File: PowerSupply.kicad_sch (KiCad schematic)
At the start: 18 parts, among them Q2 AO3401A, U4 RT7272BGSP

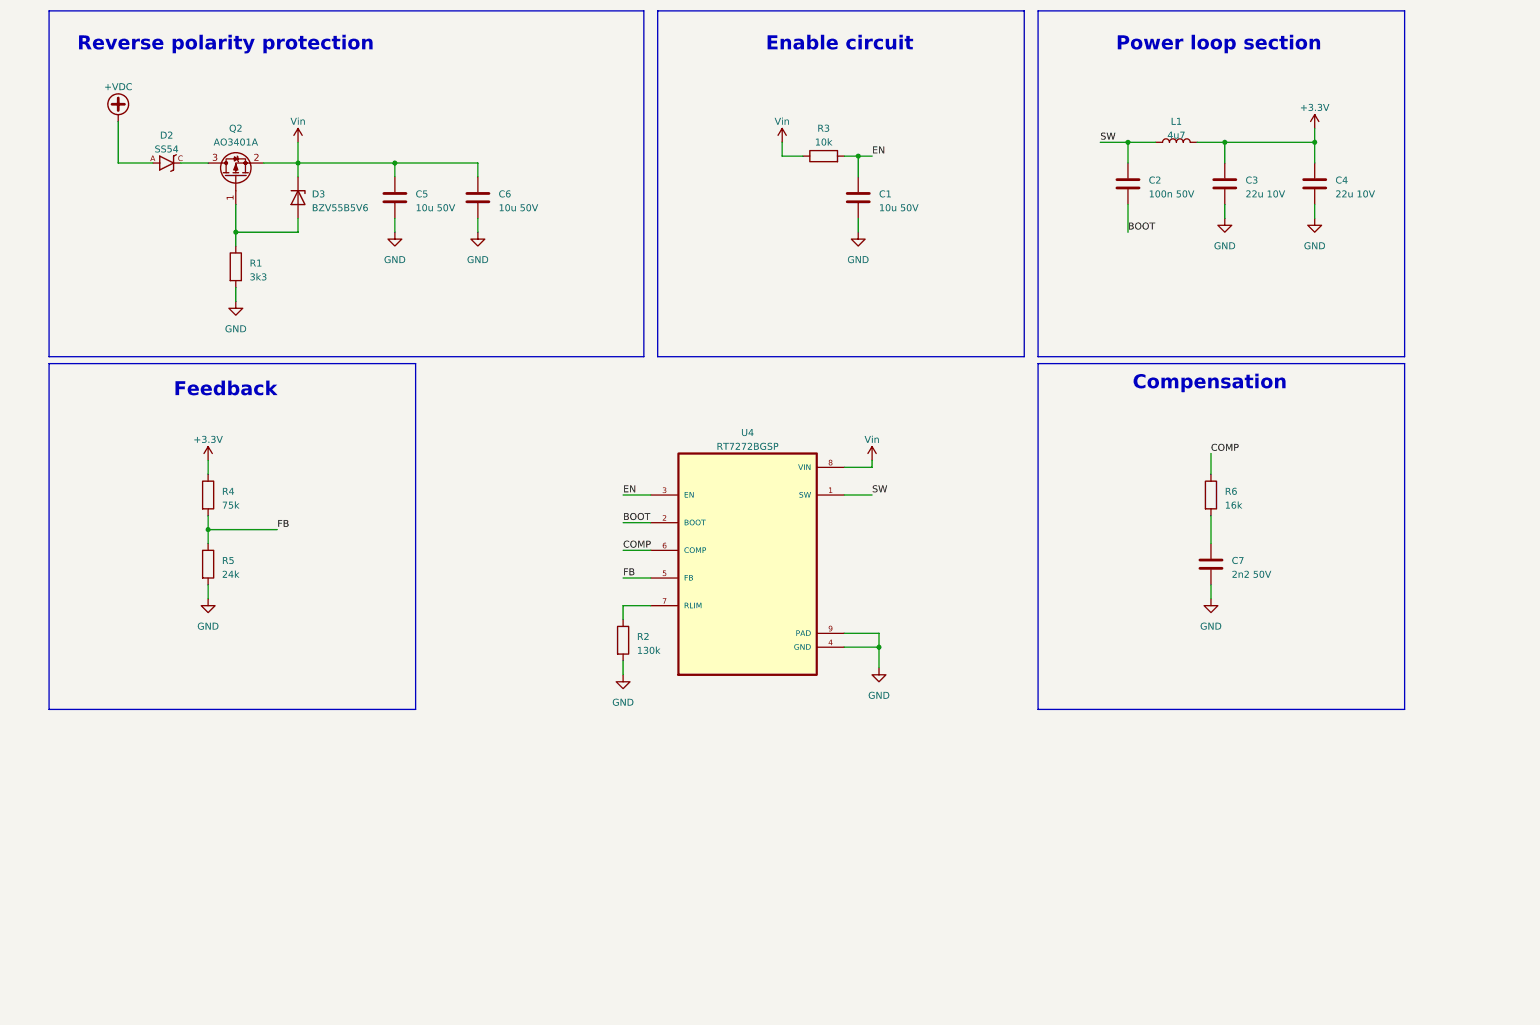
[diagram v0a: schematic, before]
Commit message: All components have been added
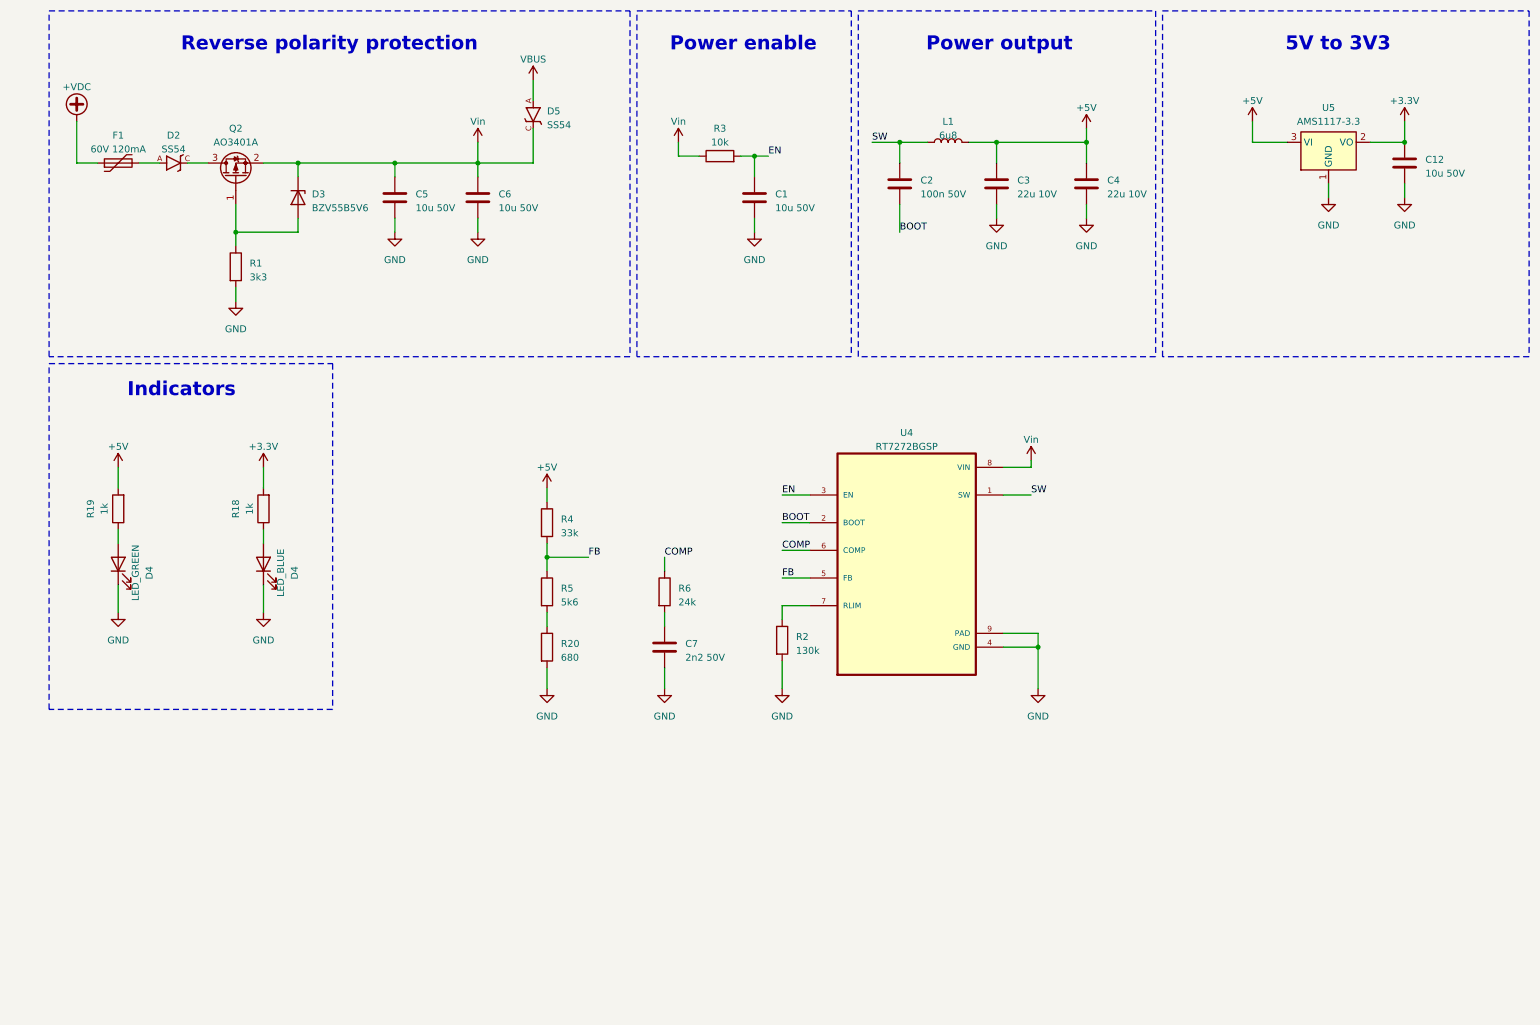
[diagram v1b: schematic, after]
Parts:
- added C12: 10u 50V, Capacitor_SMD:C_1206_3216Metric, symbol Device:C
- added D4: LED_BLUE, LED_SMD:LED_0603_1608Metric, symbol Device:LED
- added D4: LED_GREEN, LED_SMD:LED_0603_1608Metric, symbol Device:LED
- added D5: SS54, DO-214AC, symbol SS54:SS54
- added F1: 60V 120mA, Fuse:Fuse_1206_3216Metric, symbol Device:Polyfuse
- added R18, R19: 1k, Resistor_SMD:R_0402_1005Metric, symbol Device:R
- added R20: 680, Resistor_SMD:R_0402_1005Metric, symbol Device:R
- added U5: AMS1117-3.3, Package_TO_SOT_SMD:SOT-223-3_TabPin2, symbol Regulator_Linear:AMS1117-3.3
- L1: value 4u7 -> 6u8; footprint Library:IND_ASPI-0530LR-3R3M-T2 -> Inductor_SMD:L_Chilisin_BMRx00060630; LCSC C325964 -> C128690
- R4: value 75k -> 33k; LCSC C25798 -> C25779
- R5: value 24k -> 5k6; LCSC C25769 -> C25908
- R6: value 16k -> 24k; footprint Resistor_SMD:R_0805_2012Metric -> Resistor_SMD:R_0402_1005Metric; LCSC C17490 -> C25769
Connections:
- net +3.3V: now also C12.1, R18.2, U5.2 (VO); no longer C3.1, C4.1, L1.2, R4.1
- net +VDC: now also F1.1; no longer D2.A
- net GND: now also C12.2, D4.1 (K), D4.1 (K), R20.2, U5.1 (GND); no longer R5.2
- net VCC: now also D5.C
- new net: D2.A, F1.2
- new net: D4.2 (A), R19.1
- new net: D4.2 (A), R18.1
- new net: R20.1, R5.2
- new net +5V: C3.1, C4.1, L1.2, R19.2, R4.1, U5.3 (VI)
- new net VBUS: D5.A
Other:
- note added: "5V to 3V3"
- note added: "Indicators"
- note added: "Power enable"
- note added: "Power output"
- note removed: "Compensation"
- note removed: "Enable circuit"
- note removed: "Feedback"
- note removed: "Power loop section"
- moved on the sheet: C1, C2, C3, C4, C7, D2, L1, R2, R3, R4, R5, R6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

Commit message: DPB mainboard_v1 completed
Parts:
- removed D5: SS54, DO-214AC, symbol SS54:SS54
- added C2: 100n 50V, Capacitor_SMD:C_01005_0402Metric, symbol Device:C
- added D5, D6: 1N5819WS, Diode_SMD:D_SOD-323, symbol Diode:1N5819WS
- added R11: 10k, Resistor_SMD:R_0402_1005Metric, symbol Device:R
- added R12: 1k, Resistor_SMD:R_0402_1005Metric, symbol Device:R
- renumbered C12 to C10, C5 to C3, C6 to C4, C7 to C5, C1 to C6, C2 to C7, C3 to C8, C4 to C9, D3 to D4, Q2 to Q1, R19 to R10, R1 to R13, R18 to R14, R4 to R15, R5 to R16, R20 to R17, R6 to R18, R3 to R19, R2 to R20, U4 to U2, U5 to U3
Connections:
- net GND: now also C2.2, R12.1
- net VBUS: now also D5.2 (A)
- net VCC: now also D5.1 (K), D6.1 (K), R11.1
- new net V_ADC2: C2.1, R11.2, R12.2
- new net V_USB: D6.2 (A)
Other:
- note added: "Input voltage check"

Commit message: On production | V0.1
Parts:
- D5, D6: LCSC (none) -> C191023
- Q1: LCSC C2891730 -> C15127
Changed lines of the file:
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@@
+      (effects (font (size 1.27 1.27)) hide)
+    )
+    (property "LCSC" "C191023" (at 91.44 33.02 0)
       (effects (font (size 1.27 1.27)) hide)
     )
@@
       (effects (font (size 1.27 1.27)) (justify left) hide)
     )
-    (property "LCSC" "C2891730" (at 46.99 43.18 0)
+    (property "LCSC" "C15127" (at 46.99 43.18 0)
       (effects (font (size 1.27 1.27)) hide)
     )
@@
       (effects (font (size 1.27 1.27)) hide)
     )
+    (property "LCSC" "C191023" (at 76.2 33.02 0)
+      (effects (font (size 1.27 1.27)) hide)
+    )

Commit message: Add hysteresis to IR sensor. Update README file.
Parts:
- C2, C7: footprint Capacitor_SMD:C_01005_0402Metric -> Capacitor_SMD:C_0402_1005Metric
- R20: LCSC C22795 -> C93946
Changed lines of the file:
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@@
       (effects (font (size 1.27 1.27)) hide)
     )
-    (property "LCSC" "C22795" (at 147.32 128.27 0)
+    (property "LCSC" "C93946" (at 147.32 128.27 0)
       (effects (font (size 1.27 1.27)) hide)
     )
@@
       (effects (font (size 1.27 1.27)) (justify left))
     )
-    (property "Footprint" "Capacitor_SMD:C_01005_0402Metric" (at 169.8752 48.26 0)
+    (property "Footprint" "Capacitor_SMD:C_0402_1005Metric" (at 169.8752 48.26 0)
       (effects (font (size 1.27 1.27)) hide)
     )
@@
       (effects (font (size 1.27 1.27)) (justify left))
     )
-    (property "Footprint" "Capacitor_SMD:C_01005_0402Metric" (at 39.0652 179.07 0)
-      (effects (font (size 1.27 1.27)) hide)
-    )
+    (property "Footprint" "Capacitor_SMD:C_0402_1005Metric" (at 39.0652 179.07 0)
+      (effects (font (size 1.27 1.27)) hide)
+    )
